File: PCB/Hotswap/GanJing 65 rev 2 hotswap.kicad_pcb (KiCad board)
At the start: 2 copper layers, 323.9 x 95.2 mm, 138 parts, among them SW1 EC11_rotary_encoder, U1 Elite-C

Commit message: Adding new images
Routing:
- net row_4: track 362.3 -> 358.2 mm
- net row_3: track 349.2 -> 350.3 mm
- net GND: vias 112 -> 113

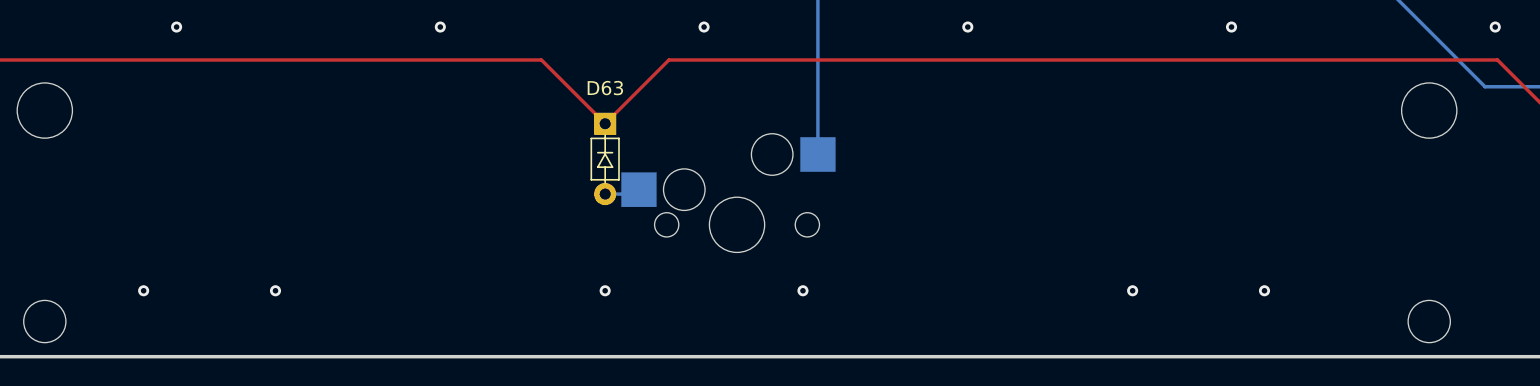
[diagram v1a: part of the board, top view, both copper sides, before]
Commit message: Adding split spacebar to hotswap PCB
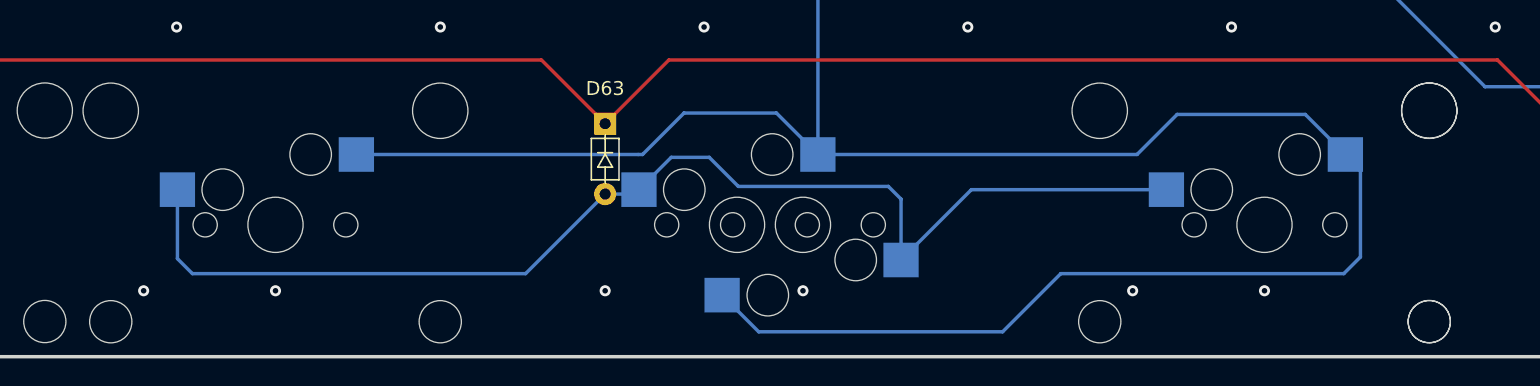
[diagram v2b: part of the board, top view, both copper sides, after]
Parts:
- added MX71: MX_2.75u_no_LED_flipped_stabs, GanJing_components:MX_2.75u_no_LED_hotswap_flipped_stabs, F.Cu at (147.6, 181.0)
- added MX72: MX_1.25u_no_LED, GanJing_components:MX_1.25u_no_LED_hotswap, F.Cu at (185.7, 181.0)
- added MX73: MX_2.25u_no_LED_flipped_stabs, GanJing_components:MX_2.25u_no_LED_hotswap_flipped_stabs, F.Cu at (219.1, 181.0)
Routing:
- net col_7: track 273.2 -> 407.0 mm
- net Net-(D63-Pad2): track 2.57 -> 88.1 mm

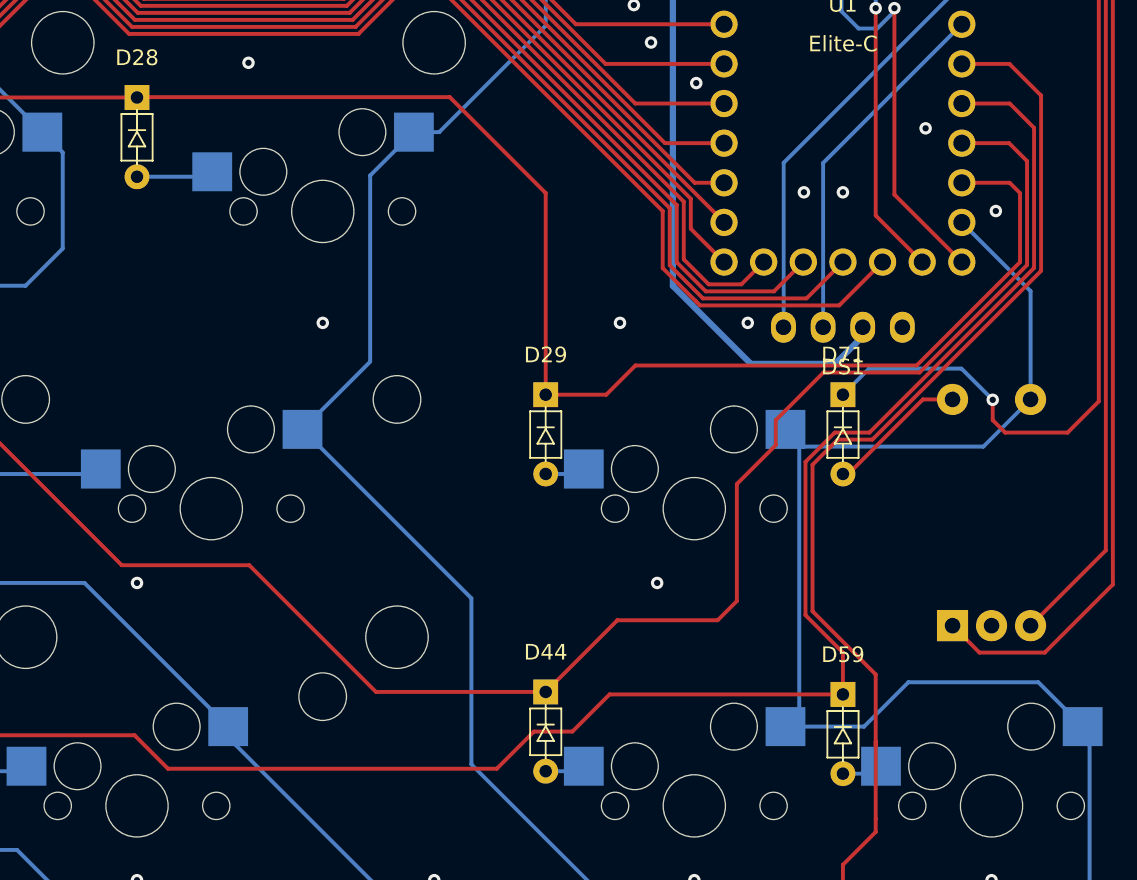
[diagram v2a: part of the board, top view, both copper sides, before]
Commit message: Fixing hotswap PCB traces
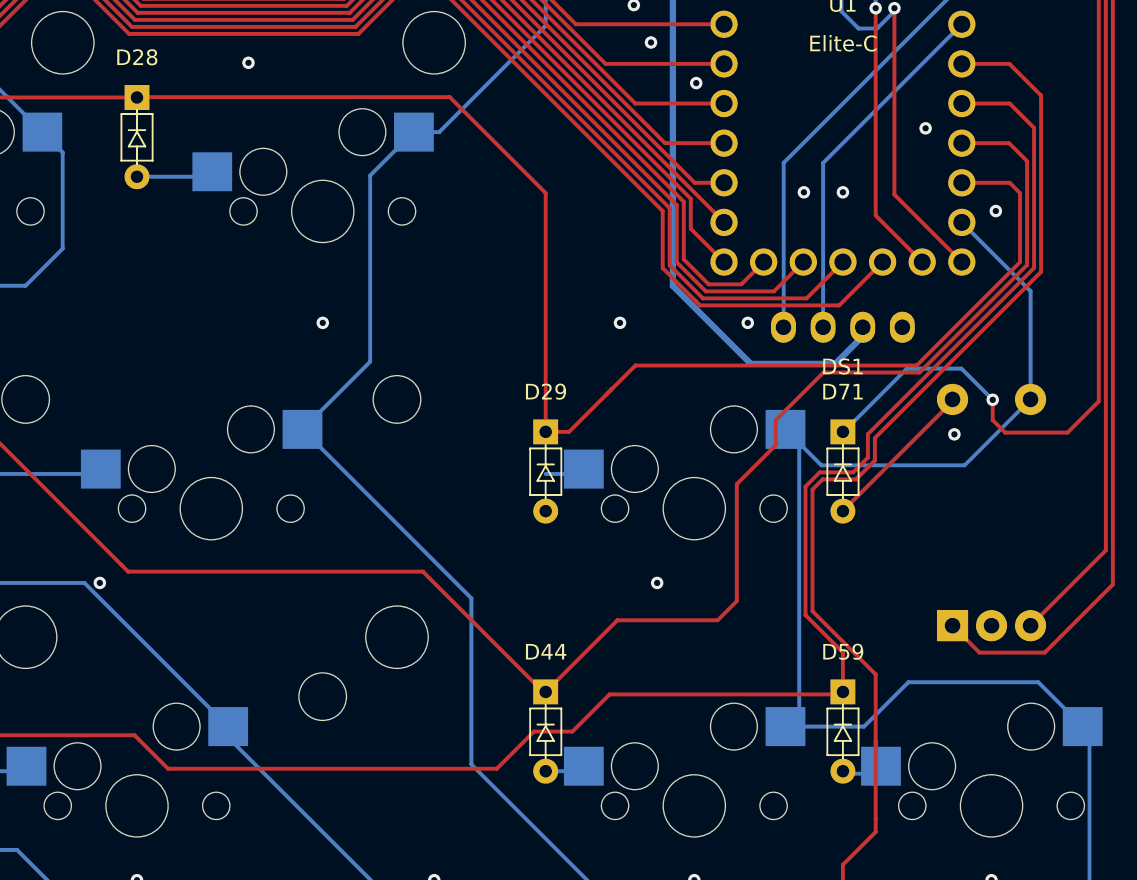
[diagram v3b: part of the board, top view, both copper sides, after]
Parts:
- moved D29 2.38 mm to (335.8, 140.5)
- moved D71 2.38 mm to (354.8, 140.5)
- moved D59 0.16 mm to (354.8, 157.2)
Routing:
- net row_2: track 341.2 -> 345.1 mm
- net S2: track 9.17 -> 10.2 mm
- net S1: track 91.2 -> 92.2 mm
- net row_1: track 377.8 -> 378.8 mm
- net GND: vias 113 -> 114

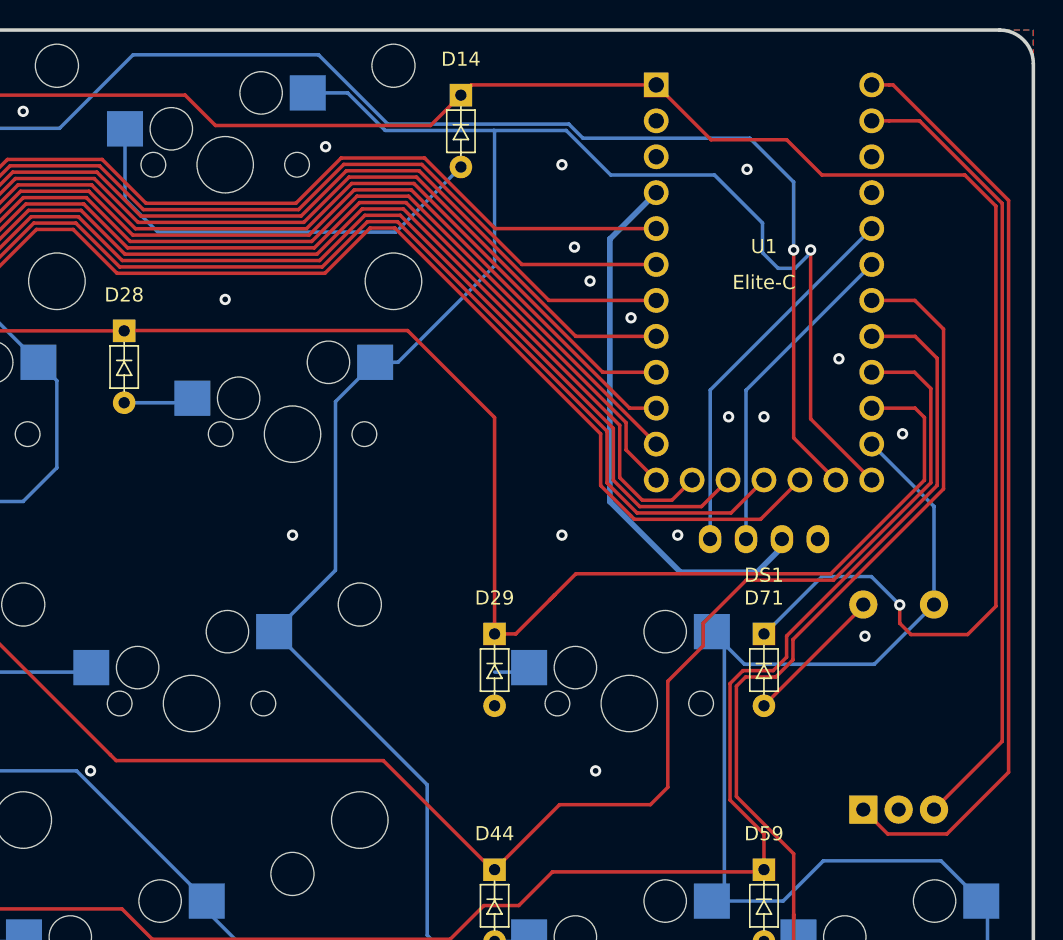
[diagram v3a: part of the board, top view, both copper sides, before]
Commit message: Updated PCBs to adjust the location of the encoder plus fix routing errors in the hotswap version. Plate file is also completed, case files still need to be finalized
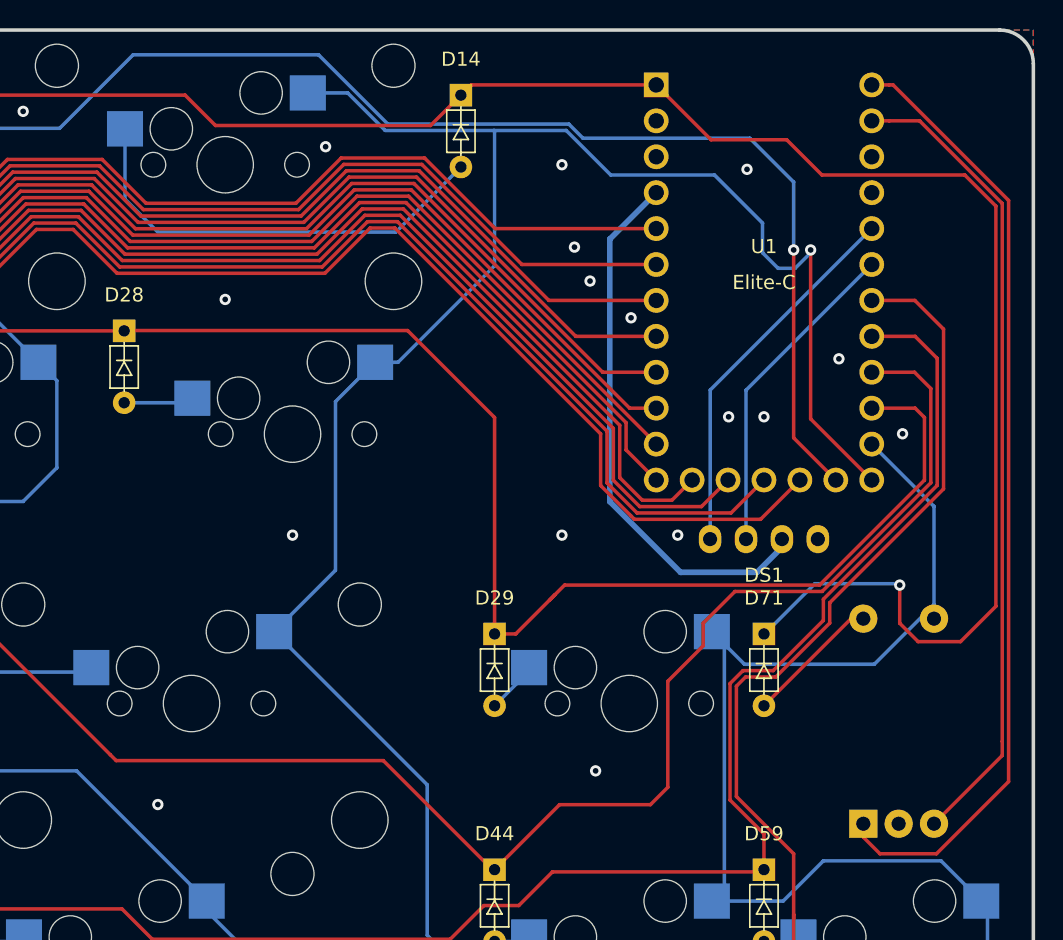
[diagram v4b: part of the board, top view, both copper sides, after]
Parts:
- moved SW1 1.00 mm to (364.3, 143.9)
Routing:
- net rotory_1: track 66.3 -> 68.0 mm
- net Net-(D29-Pad2): track 2.57 -> 4.16 mm
- net rotory_2: track 56.5 -> 57.5 mm
- net row_1: track 378.8 -> 379.6 mm
- net S2: track 10.2 -> 9.59 mm
- net GND: vias 114 -> 113

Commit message: Switching to KiCad 6.0.1 so some files have been converted and the component symbol library files has been converted from .lib to .kicad_sym
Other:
- board size 323.9 x 95.2 mm -> 323.8 x 95.2 mm
- net class Default removed
